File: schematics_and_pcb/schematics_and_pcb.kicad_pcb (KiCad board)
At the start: 2 copper layers, 46 parts, among them J1 RND 205-00623, J2 RND 205-00627, SW1 RND 210-00210, U1 MIC5235YM5-TR, U2 AP2125N-3.3TRG1, U4 STM32F411RETx, Y1 YLFXTAL029370

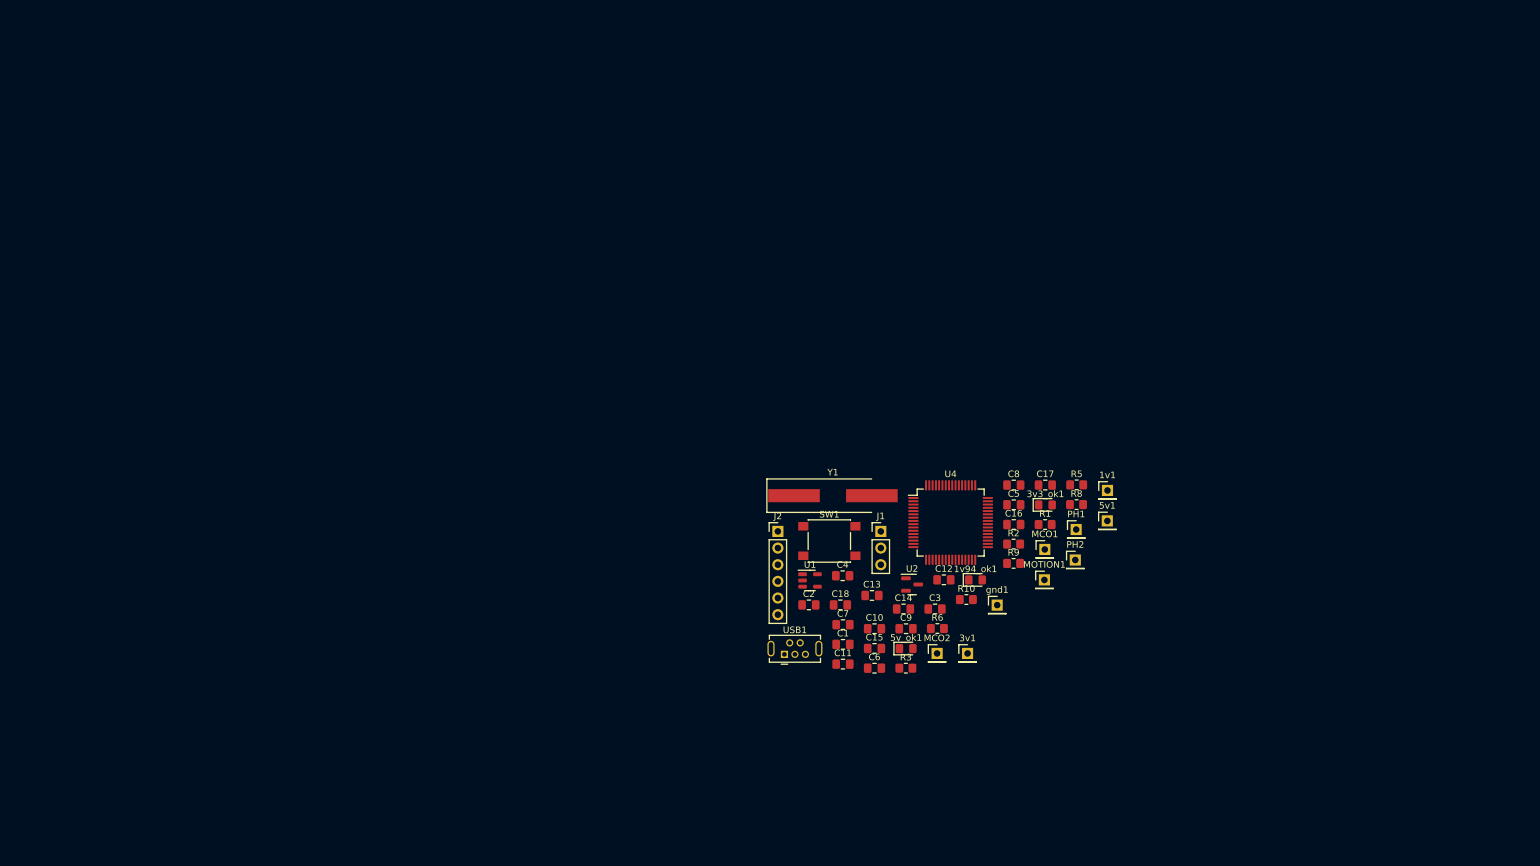
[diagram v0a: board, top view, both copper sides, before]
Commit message: done with main board outline
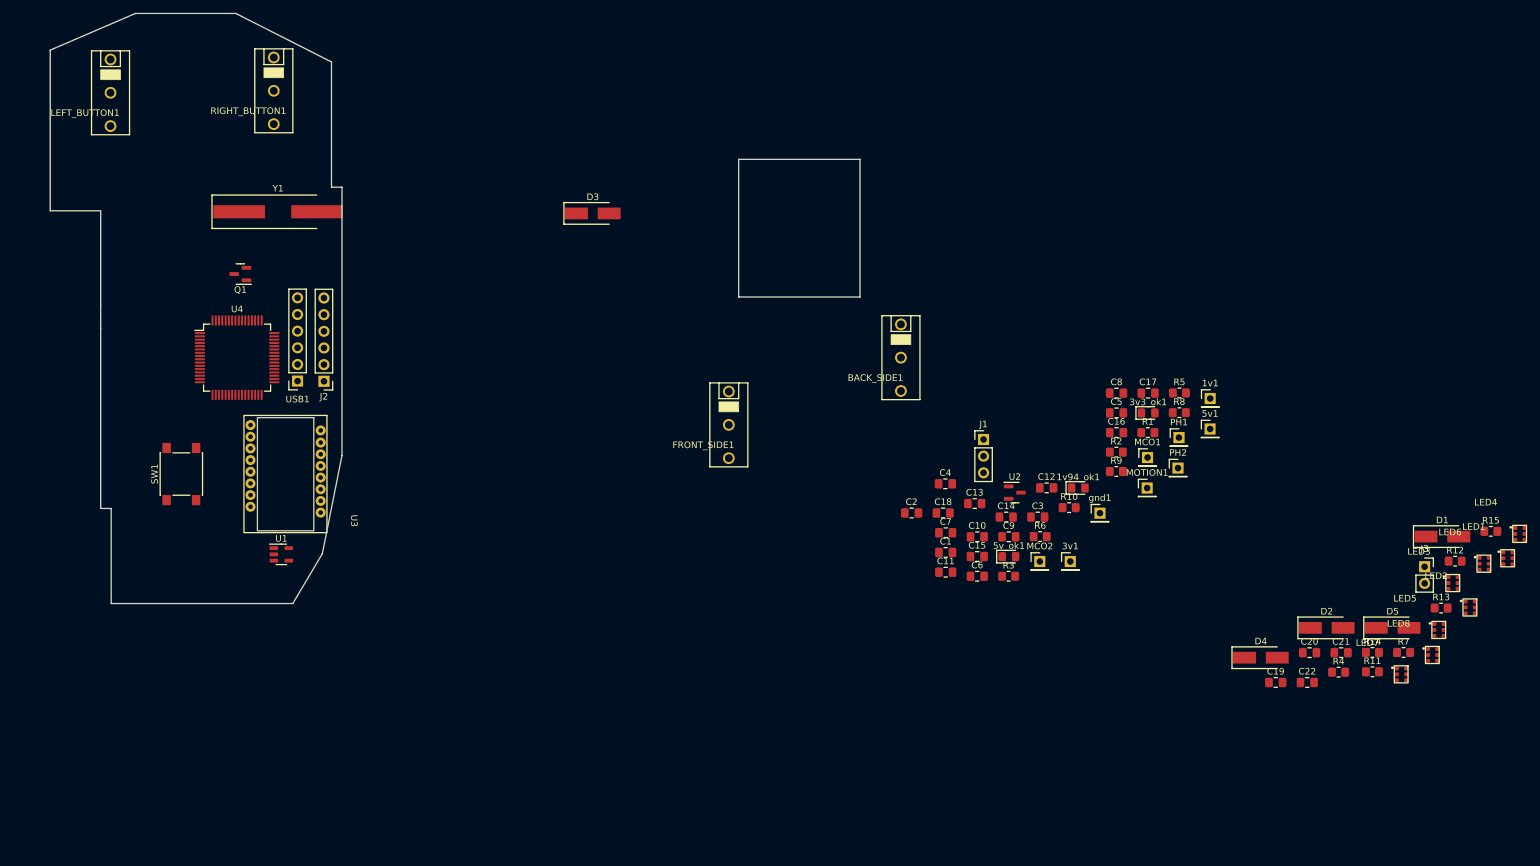
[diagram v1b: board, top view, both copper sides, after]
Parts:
- added BACK_SIDE1: D2F-01F, mouse:D2F-01F, F.Cu at (146.2, 66.5)
- added C19: 10u, Capacitor_SMD:C_0805_2012Metric_Pad1.18x1.45mm_HandSolder, F.Cu at (203.4, 116.0)
- added C20: 10u, Capacitor_SMD:C_0805_2012Metric_Pad1.18x1.45mm_HandSolder, F.Cu at (208.6, 111.5)
- added C21: 10u, Capacitor_SMD:C_0805_2012Metric_Pad1.18x1.45mm_HandSolder, F.Cu at (213.4, 111.5)
- added C22: 10u, Capacitor_SMD:C_0805_2012Metric_Pad1.18x1.45mm_HandSolder, F.Cu at (208.2, 116.0)
- added D1: S1A, Diode_SMD:D_SMA_Handsoldering, F.Cu at (228.8, 93.8)
- added D2: 1N4001, Diode_SMD:D_SMA_Handsoldering, F.Cu at (211.2, 107.7)
- added D3: S1A, Diode_SMD:D_SMA_Handsoldering, F.Cu at (99.2, 44.5)
- added D4: S1A, Diode_SMD:D_SMA_Handsoldering, F.Cu at (201.1, 112.3)
- added D5: S1A, Diode_SMD:D_SMA_Handsoldering, F.Cu at (221.2, 107.7)
- added FRONT_SIDE1: D2F-01F, mouse:D2F-01F, F.Cu at (120.0, 76.8)
- added J3: Motor con, Connector_PinSocket_2.54mm:PinSocket_1x02_P2.54mm_Vertical, F.Cu at (226.1, 98.4)
- added LED1: RND_135-00249, mouse:RND_135-00249, F.Cu at (238.8, 97.1)
- added LED2: RND_135-00249, mouse:RND_135-00249, F.Cu at (233.1, 104.6)
- added LED3: RND_135-00249, mouse:RND_135-00249, F.Cu at (230.5, 100.9)
- added LED4: RND_135-00249, mouse:RND_135-00249, F.Cu at (240.7, 93.4)
- added LED5: RND_135-00249, mouse:RND_135-00249, F.Cu at (228.3, 108.0)
- added LED6: RND_135-00249, mouse:RND_135-00249, F.Cu at (235.2, 97.9)
- added LED7: RND_135-00249, mouse:RND_135-00249, F.Cu at (222.6, 114.8)
- added LED8: RND_135-00249, mouse:RND_135-00249, F.Cu at (227.3, 111.8)
- added LEFT_BUTTON1: D2F-01F, mouse:D2F-01F, F.Cu at (25.7, 26.1)
- added Q1: PMV213SN, Package_TO_SOT_SMD:SOT-23, F.Cu at (45.5, 53.8)
- added R11: 4.7k, Resistor_SMD:R_0805_2012Metric_Pad1.20x1.40mm_HandSolder, F.Cu at (218.2, 114.4)
- added R12: 4.7k, Resistor_SMD:R_0805_2012Metric_Pad1.20x1.40mm_HandSolder, F.Cu at (230.8, 97.5)
- added R13: 1K, Resistor_SMD:R_0805_2012Metric_Pad1.20x1.40mm_HandSolder, F.Cu at (228.6, 104.7)
- added R14: 10k, Resistor_SMD:R_0805_2012Metric_Pad1.20x1.40mm_HandSolder, F.Cu at (218.2, 111.5)
- added R15: 10k, Resistor_SMD:R_0805_2012Metric_Pad1.20x1.40mm_HandSolder, F.Cu at (236.2, 93.0)
- added R4: 4.7k, Resistor_SMD:R_0805_2012Metric_Pad1.20x1.40mm_HandSolder, F.Cu at (213.0, 114.5)
- added R7: 4.7k, Resistor_SMD:R_0805_2012Metric_Pad1.20x1.40mm_HandSolder, F.Cu at (222.9, 111.5)
- added RIGHT_BUTTON1: D2F-01F, mouse:D2F-01F, F.Cu at (50.6, 25.8)
- added U3: PWM3389DM-T3QU, mouse:PMW3389DM-T3QU, F.Cu at (47.0, 89.2)
- USB1: footprint Connector_USB:USB_Mini-B_Tensility_54-00023_Vertical -> Connector_PinSocket_2.54mm:PinSocket_1x06_P2.54mm_Vertical
- moved U4 111.7 mm to (45.0, 66.5)
- moved SW1 99.4 mm to (36.5, 84.2), turned to 90 degrees
- moved Y1 95.1 mm to (51.2, 44.2)
- moved USB1 85.2 mm to (54.2, 70.1), turned to 180 degrees
- moved U1 80.7 mm to (51.8, 96.5)
- moved J2 72.9 mm to (58.2, 70.1), turned to 180 degrees
- moved 5v1 21.0 mm to (193.4, 77.4)
- moved C1 21.0 mm to (153.1, 96.2)
- moved MOTION1 21.0 mm to (183.8, 86.4)
- moved 3v1 21.0 mm to (172.1, 97.6)
- moved 3v3_ok1 21.0 mm to (184.0, 74.9)
- moved 5v_ok1 21.0 mm to (162.7, 96.8)
- moved C11 21.0 mm to (153.1, 99.2)
- moved C14 21.0 mm to (162.3, 90.8)
- moved C3 21.0 mm to (167.1, 90.8)
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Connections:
- U4 pad 56: unconnected-(U4-Pad56) -> LEFT_STATE
- U4 pad 57: unconnected-(U4-Pad57) -> RIGHT_STATE
- U4 pad 58: unconnected-(U4-Pad58) -> FRONT_STATE
- U4 pad 59: unconnected-(U4-Pad59) -> BACK_STATE
- U4 pad 61: unconnected-(U4-Pad61) -> PHASE_A
- U4 pad 62: unconnected-(U4-Pad62) -> PHASE_B
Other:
- board outline added: 123.5 x 90 mm

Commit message: main board outline tuned
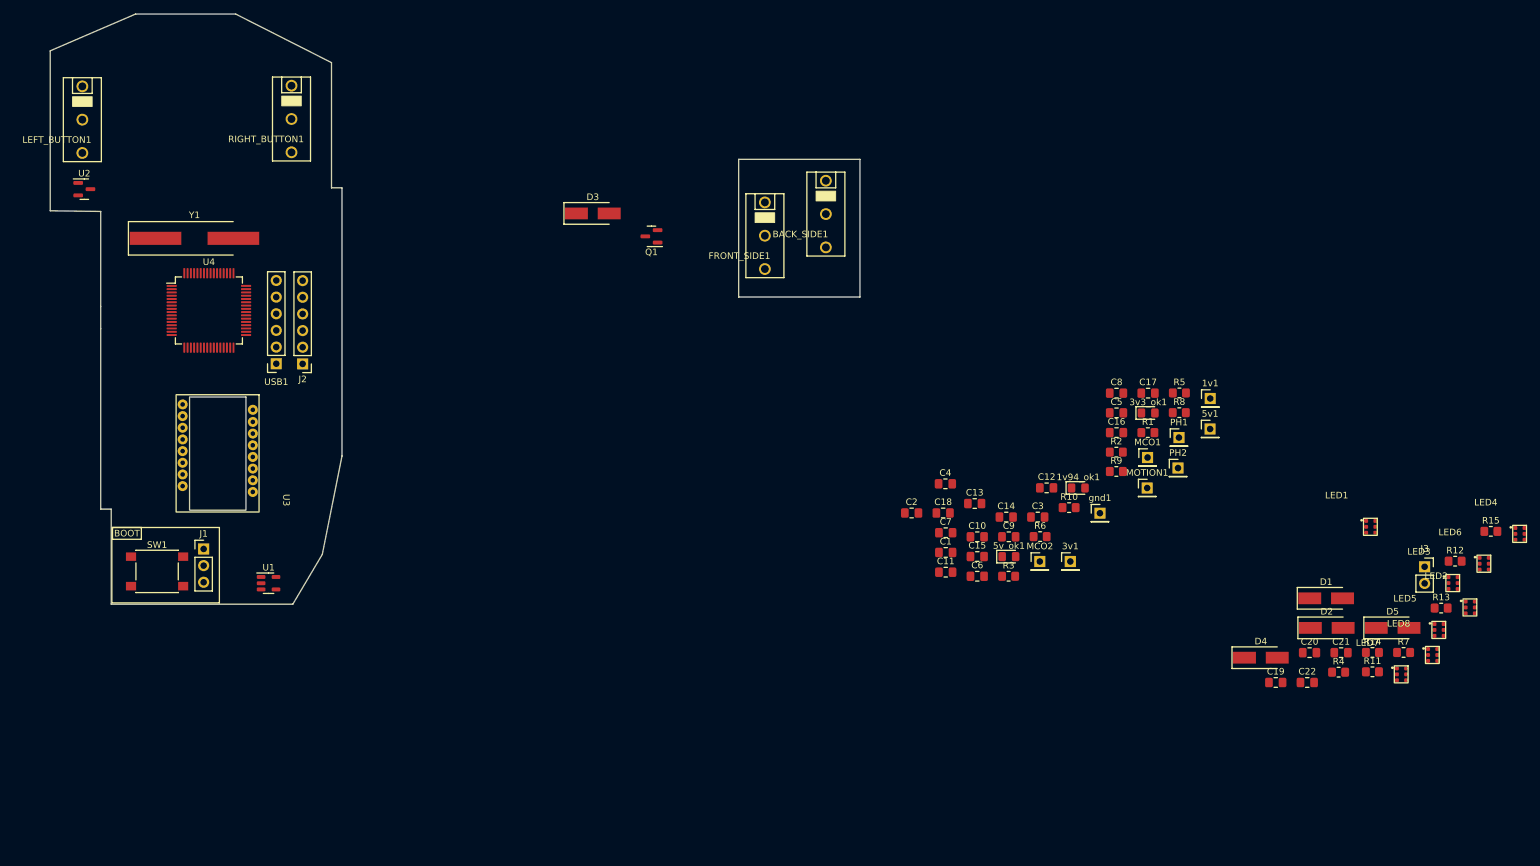
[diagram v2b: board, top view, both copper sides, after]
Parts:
- moved U2 149.3 mm to (21.7, 40.8)
- moved J1 120.1 mm to (39.9, 95.7)
- moved Q1 63.0 mm to (108.2, 48.0)
- moved FRONT_SIDE1 29.4 mm to (125.5, 47.9)
- moved BACK_SIDE1 24.7 mm to (134.8, 44.6)
- moved LED1 21.5 mm to (217.9, 92.3)
- moved D1 20.1 mm to (211.1, 103.2)
- moved SW1 15.3 mm to (32.8, 99.1), turned to 0 degrees
- moved Y1 13.4 mm to (38.5, 48.3)
- moved U3 10.8 mm to (36.7, 86.1)
- moved U4 8.39 mm to (40.7, 59.3)
- moved LEFT_BUTTON1 5.94 mm to (21.4, 30.2)
- moved RIGHT_BUTTON1 5.08 mm to (53.3, 30.1)
- moved U1 4.81 mm to (49.8, 100.9)
- moved USB1 4.19 mm to (51.0, 67.4)
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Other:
- outline, holes or cut-outs redrawn
- board text added: "BOOT"
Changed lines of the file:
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@@
   )
   (footprint "mouse:PMW3389DM-T3QU" (layer "F.Cu")
-    (at 47.05 89.24 -90)
+    (at 36.7 86.09 -90)
     (property "Sheetfile" "schematics_and_pcb.kicad_sch")
     (property "Sheetname" "")
@@
   )
   (footprint "Button_Switch_SMD:SW_Push_1P1T_NO_6x6mm_H9.5mm" (layer "F.Cu")
-    (at 36.5 84.25 90)
+    (at 32.8 99.1)
     (descr "tactile push button, 6x6mm e.g. PTS645xx series, height=9.5mm")
     (tags "tact sw push 6mm smd")
@@
     (property "Sheetname" "")
     (attr smd)
-    (fp_text reference "SW1" (at 0 -4.05 90) (layer "F.SilkS")
-      (effects (font (size 1 1) (thickness 0.15)))
-    )
-    (fp_text value "RND 210-00210" (at 0 4.15 90) (layer "F.Fab")
-      (effects (font (size 1 1) (thickness 0.15)))
-    )
-    (fp_text user "${REFERENCE}" (at 0 -4.05 90) (layer "F.Fab")
+    (fp_text reference "SW1" (at 0 -4.05) (layer "F.SilkS")
+      (effects (font (size 1 1) (thickness 0.15)))
+    )
+    (fp_text value "RND 210-00210" (at 0 4.15) (layer "F.Fab")
+      (effects (font (size 1 1) (thickness 0.15)))
+    )
+    (fp_text user "${REFERENCE}" (at 0 -4.05) (layer "F.Fab")
       (effects (font (size 1 1) (thickness 0.15)))
     )
@@
     (fp_line (start -3 -3) (end -3 3) (layer "F.Fab") (width 0.1))
     (fp_circle (center 0 0) (end 1.75 -0.05) (layer "F.Fab") (width 0.1) (fill none))
-    (pad "1" smd rect (at -3.975 -2.25 90) (size 1.55 1.3) (layers "F.Cu" "F.Paste" "F.Mask")
+    (pad "1" smd rect (at -3.975 -2.25) (size 1.55 1.3) (layers "F.Cu" "F.Paste" "F.Mask")
       (net 9 "NRST") (pinfunction "1") (pintype "passive"))
-    (pad "1" smd rect (at 3.975 -2.25 90) (size 1.55 1.3) (layers "F.Cu" "F.Paste" "F.Mask")
+    (pad "1" smd rect (at 3.975 -2.25) (size 1.55 1.3) (layers "F.Cu" "F.Paste" "F.Mask")
       (net 9 "NRST") (pinfunction "1") (pintype "passive"))
-    (pad "2" smd rect (at -3.975 2.25 90) (size 1.55 1.3) (layers "F.Cu" "F.Paste" "F.Mask")
+    (pad "2" smd rect (at -3.975 2.25) (size 1.55 1.3) (layers "F.Cu" "F.Paste" "F.Mask")
       (net 2 "GND") (pinfunction "2") (pintype "passive"))
-    (pad "2" smd rect (at 3.975 2.25 90) (size 1.55 1.3) (layers "F.Cu" "F.Paste" "F.Mask")
+    (pad "2" smd rect (at 3.975 2.25) (size 1.55 1.3) (layers "F.Cu" "F.Paste" "F.Mask")
       (net 2 "GND") (pinfunction "2") (pintype "passive"))
     (model "${KICAD6_3DMODEL_DIR}/Button_Switch_SMD.3dshapes/SW_PUSH_6mm_H9.5mm.wrl"
@@
   )
   (footprint "Package_QFP:LQFP-64_10x10mm_P0.5mm" (layer "F.Cu")
-    (at 45 66.5)
+    (at 40.7 59.3)
     (descr "LQFP, 64 Pin (https://www.analog.com/media/en/technical-documentation/data-sheets/ad7606_7606-6_7606-4.pdf), generated with kicad-footprint-generator ipc_gullwing_generator.py")
     (tags "LQFP QFP")
@@
   )
   (footprint "Package_TO_SOT_SMD:SOT-23" (layer "F.Cu")
-    (at 163.62 87.08)
+    (at 21.7 40.8)
     (descr "SOT, 3 Pin (https://www.jedec.org/system/files/docs/to-236h.pdf variant AB), generated with kicad-footprint-generator ipc_gullwing_generator.py")
     (tags "SOT TO_SOT_SMD")
@@
   )
   (footprint "Diode_SMD:D_SMA_Handsoldering" (layer "F.Cu")
-    (at 228.8215 93.7915)
+    (at 211.1 103.2)
     (descr "Diode SMA (DO-214AC) Handsoldering")
     (tags "Diode SMA (DO-214AC) Handsoldering")
@@
   )
   (footprint "Package_TO_SOT_SMD:SOT-23-5" (layer "F.Cu")
-    (at 51.75 96.5)
+    (at 49.8 100.9)
     (descr "SOT, 5 Pin (https://www.jedec.org/sites/default/files/docs/Mo-178c.PDF variant AA), generated with kicad-footprint-generator ipc_gullwing_generator.py")
     (tags "SOT TO_SOT_SMD")
@@
   )
   (footprint "mouse:D2F-01F" (layer "F.Cu")
-    (at 120 76.75)
+    (at 125.5 47.9)
     (property "Sheetfile" "schematics_and_pcb.kicad_sch")
     (property "Sheetname" "")
@@
   )
   (footprint "mouse:D2F-01F" (layer "F.Cu")
-    (at 146.25 66.5)
+    (at 134.8 44.6)
     (property "Sheetfile" "schematics_and_pcb.kicad_sch")
     (property "Sheetname" "")
@@
   )
   (footprint "mouse:D2F-01F" (layer "F.Cu")
-    (at 25.7 26.1)
+    (at 21.4 30.2)
     (property "Sheetfile" "schematics_and_pcb.kicad_sch")
     (property "Sheetname" "")
@@
   )
   (footprint "Crystal:Crystal_SMD_HC49-SD_HandSoldering" (layer "F.Cu")
-    (at 51.25 44.25)
+    (at 38.5 48.3)
     (descr "SMD Crystal HC-49-SD http://cdn-reichelt.de/documents/datenblatt/B400/xxx-HC49-SMD.pdf, hand-soldering, 11.4x4.7mm^2 package")
     (tags "SMD SMT crystal hand-soldering")
@@
   )
   (footprint "Package_TO_SOT_SMD:SOT-23" (layer "F.Cu")
-    (at 45.5 53.75 180)
+    (at 108.2 48 180)
     (descr "SOT, 3 Pin (https://www.jedec.org/system/files/docs/to-236h.pdf variant AB), generated with kicad-footprint-generator ipc_gullwing_generator.py")
     (tags "SOT TO_SOT_SMD")
@@
   )
   (footprint "Connector_PinHeader_2.54mm:PinHeader_1x03_P2.54mm_Vertical" (layer "F.Cu")
-    (at 158.85 78.98)
+    (at 39.9 95.675)
     (descr "Through hole straight pin header, 1x03, 2.54mm pitch, single row")
     (tags "Through hole pin header THT 1x03 2.54mm single row")
@@
   )
   (footprint "mouse:RND_135-00249" (layer "F.Cu")
-    (at 238.8265 97.0965)
+    (at 217.9 92.3)
     (property "Sheetfile" "schematics_and_pcb.kicad_sch")
     (property "Sheetname" "")
@@
   )
   (footprint "mouse:D2F-01F" (layer "F.Cu")
-    (at 50.6 25.8)
+    (at 53.3 30.1)
     (property "Sheetfile" "schematics_and_pcb.kicad_sch")
     (property "Sheetname" "")
@@
   )
   (footprint "Connector_PinHeader_2.54mm:PinHeader_1x06_P2.54mm_Vertical" (layer "F.Cu")
-    (at 58.25 70.1 180)
+    (at 55 67.45 180)
     (descr "Through hole straight pin header, 1x06, 2.54mm pitch, single row")
     (tags "Through hole pin header THT 1x06 2.54mm single row")
@@
   )
   (footprint "Connector_PinSocket_2.54mm:PinSocket_1x06_P2.54mm_Vertical" (layer "F.Cu")
-    (at 54.225 70.075 180)
+    (at 50.975 67.425 180)
     (descr "Through hole straight socket strip, 1x06, 2.54mm pitch, single row (from Kicad 4.0.7), script generated")
     (tags "Through hole socket strip THT 1x06 2.54mm single row")
@@
     )
   )
-  (gr_line (start 59.4 21.4) (end 59.4 40.5) (layer "Edge.Cuts") (width 0.1))
-  (gr_line (start 58 96.4) (end 61 81.4) (layer "Edge.Cuts") (width 0.1))
-  (gr_line (start 53.5 104) (end 58 96.4) (layer "Edge.Cuts") (width 0.1))
-  (gr_line (start 29.5 14) (end 16.5 19.6) (layer "Edge.Cuts") (width 0.1))
-  (gr_line (start 25.8 104) (end 53.5 104) (layer "Edge.Cuts") (width 0.1))
-  (gr_line (start 16.5 19.6) (end 16.5 44.1) (layer "Edge.Cuts") (width 0.1))
-  (gr_line (start 44.8 14) (end 59.4 21.4) (layer "Edge.Cuts") (width 0.1))
-  (gr_line (start 24.2 89.5) (end 24.2 62) (layer "Edge.Cuts") (width 0.1))
-  (gr_line (start 29.5 14) (end 44.8 14) (layer "Edge.Cuts") (width 0.1))
-  (gr_line (start 24.2 58.6) (end 24.2 62) (layer "Edge.Cuts") (width 0.1))
-  (gr_line (start 24.2 58.6) (end 24.2 44.1) (layer "Edge.Cuts") (width 0.1))
-  (gr_line (start 61 40.5) (end 61 81.4) (layer "Edge.Cuts") (width 0.1))
-  (gr_line (start 25.8 104) (end 25.8 89.5) (layer "Edge.Cuts") (width 0.1))
-  (gr_line (start 59.4 40.5) (end 61 40.5) (layer "Edge.Cuts") (width 0.1))
+  (gr_rect (start 26 92.4) (end 30.4 94.2) (layer "F.SilkS") (width 0.15) (fill none))
+  (gr_rect (start 25.9 103.9) (end 42.3 92.4) (layer "F.SilkS") (width 0.15) (fill none))
+  (gr_line (start 59.4 21.5) (end 59.4 40.6) (layer "Edge.Cuts") (width 0.1))
+  (gr_line (start 58 96.5) (end 61 81.5) (layer "Edge.Cuts") (width 0.1))
+  (gr_line (start 53.5 104.1) (end 58 96.5) (layer "Edge.Cuts") (width 0.1))
+  (gr_line (start 29.5 14.1) (end 16.5 19.7) (layer "Edge.Cuts") (width 0.1))
+  (gr_line (start 25.8 104.1) (end 53.5 104.1) (layer "Edge.Cuts") (width 0.1))
+  (gr_line (start 16.5 44.1) (end 16.5 19.7) (layer "Edge.Cuts") (width 0.1))
+  (gr_line (start 44.8 14.1) (end 59.4 21.5) (layer "Edge.Cuts") (width 0.1))
+  (gr_line (start 24.2 89.6) (end 24.2 62.1) (layer "Edge.Cuts") (width 0.1))
+  (gr_line (start 29.5 14.1) (end 44.8 14.1) (layer "Edge.Cuts") (width 0.1))
+  (gr_line (start 24.2 58.7) (end 24.2 62.1) (layer "Edge.Cuts") (width 0.1))
+  (gr_line (start 24.2 58.7) (end 24.2 44.2) (layer "Edge.Cuts") (width 0.1))
+  (gr_line (start 61 40.6) (end 61 81.5) (layer "Edge.Cuts") (width 0.1))
+  (gr_line (start 25.8 104.1) (end 25.8 89.6) (layer "Edge.Cuts") (width 0.1))
+  (gr_line (start 59.4 40.6) (end 61 40.6) (layer "Edge.Cuts") (width 0.1))
   (gr_rect (start 121.5 36.25) (end 140 57.25) (layer "Edge.Cuts") (width 0.1) (fill none))
-  (gr_line (start 16.5 44.1) (end 24.2 44.1) (layer "Edge.Cuts") (width 0.1))
-  (gr_line (start 24.2 89.5) (end 25.8 89.5) (layer "Edge.Cuts") (width 0.1))
+  (gr_line (start 16.5 44.1) (end 24.2 44.2) (layer "Edge.Cuts") (width 0.1))
+  (gr_line (start 24.2 89.6) (end 25.8 89.6) (layer "Edge.Cuts") (width 0.1))
+  (gr_text "BOOT" (at 28.2 93.3) (layer "F.SilkS")
+    (effects (font (size 1 1) (thickness 0.15)))
+  )
 )
